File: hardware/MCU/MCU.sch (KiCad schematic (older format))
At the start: 27 parts, among them P1 CONN_01X05, P2 CONN_01X04, P3 CONN_01X03, U1 MAX6369, U2 DS18B20, U3 PIC18F45K22, U4 LM358, Y1 Crystal

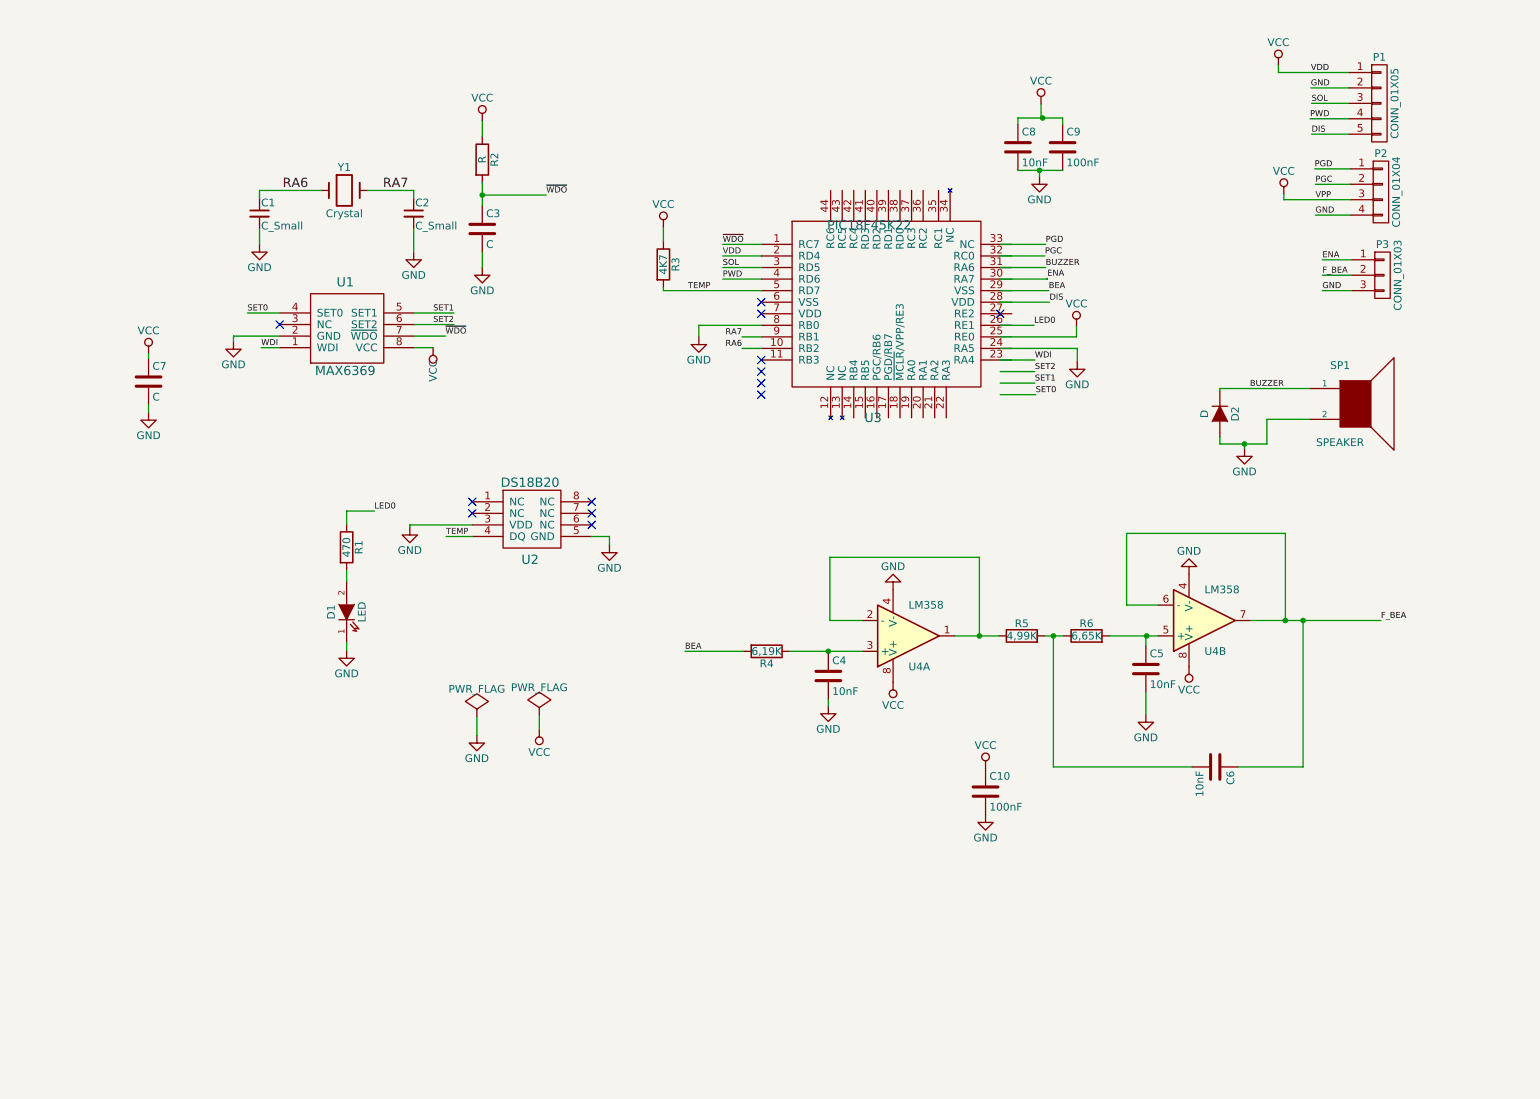
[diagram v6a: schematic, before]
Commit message: PIC schematic of 64 pins. Reorganized pinout
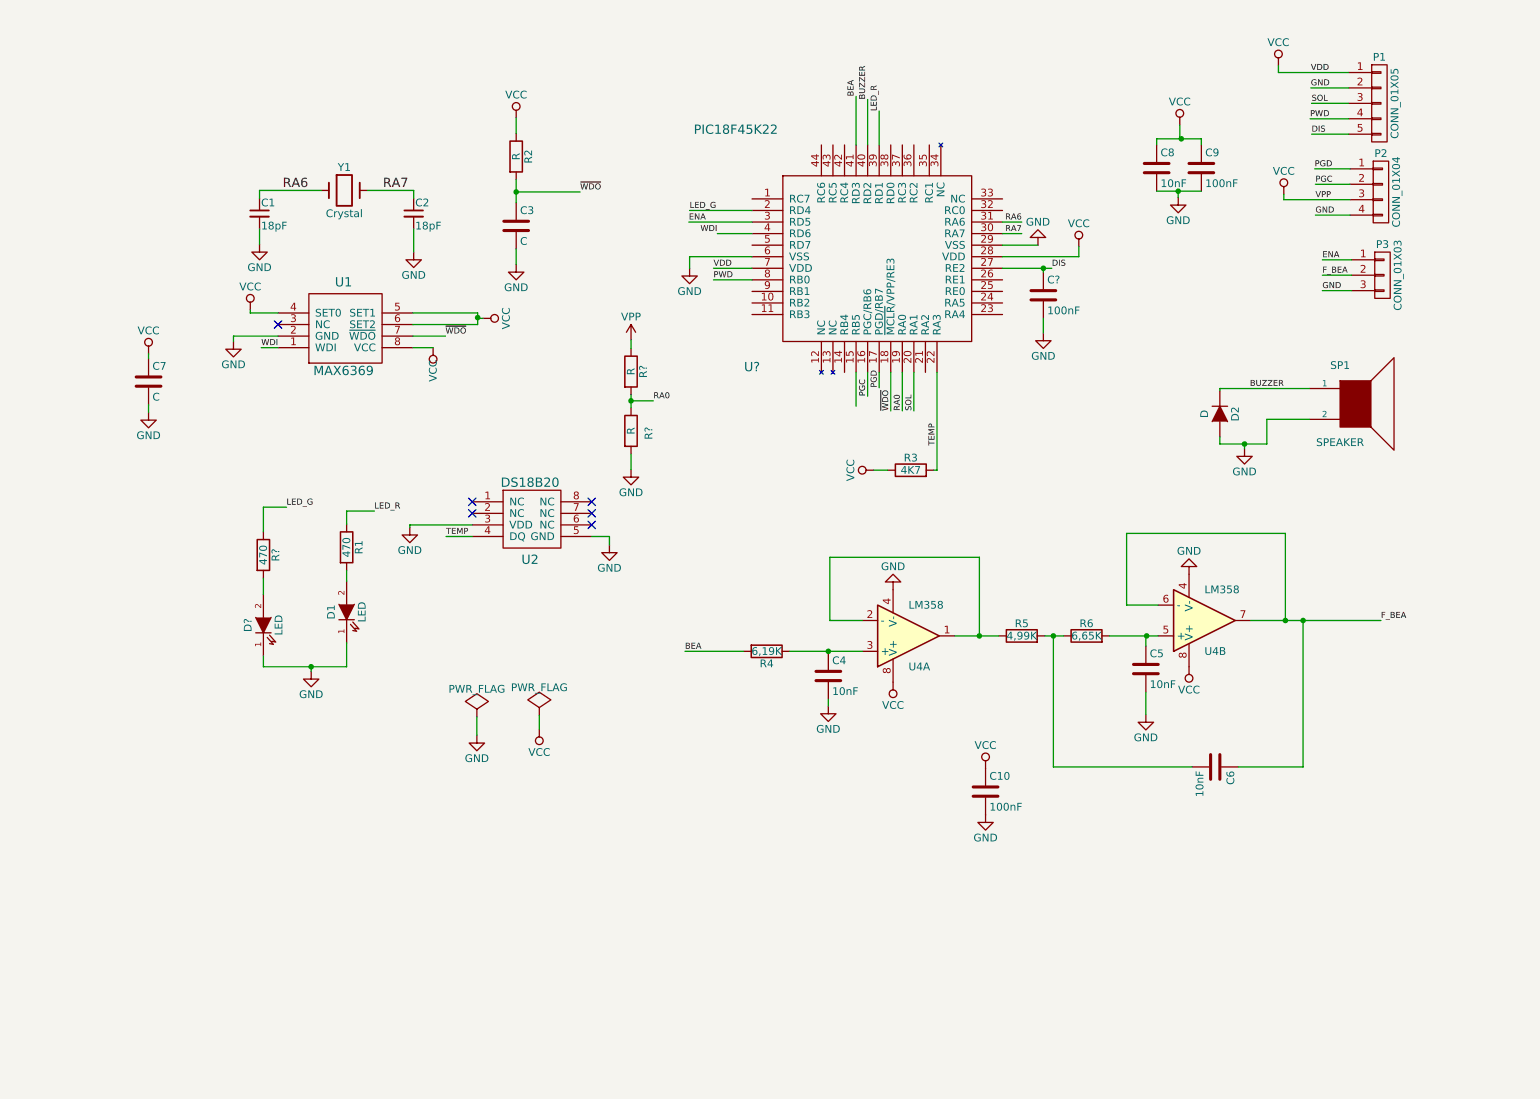
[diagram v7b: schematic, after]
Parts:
- removed U3: PIC18F45K22, Housings_SOIC:SOIC-28W_7.5x17.9mm_Pitch1.27mm, symbol PIC18F45K22
- added C?: 100nF, Capacitors_SMD:C_1206_HandSoldering, symbol C
- added D?: LED, symbol LED
- added R?: 470, Resistors_SMD:R_1206_HandSoldering, symbol R
- added R? (x2): R, symbol R
- added U?: PIC18F45K22, symbol PIC18F45K22
- C1, C2: value C_Small -> 18pF
- U1: footprint Housings_SOIC:SOIJ-8_5.3x5.3mm_Pitch1.27mm -> smd-semi:SOT-23-8
- Y1: footprint Crystals:Crystal_C26-LF_d2.1mm_l6.5mm_Horizontal -> Crystals:Crystal_HC49-4H_Vertical
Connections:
- net labels added: LED_G, LED_R, RA0
- net labels removed: LED0, SET0, SET1, SET2
- wire segments 109 -> 123
- no-connect marks 13 -> 6
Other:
- moved on the sheet: C3, C8, C9, R2, R3

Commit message: Corregidas erratas en el documento de requisitos de la MCU. Añadido regulador al esquematico y ajustadas las conexiones acorde a los requisitos
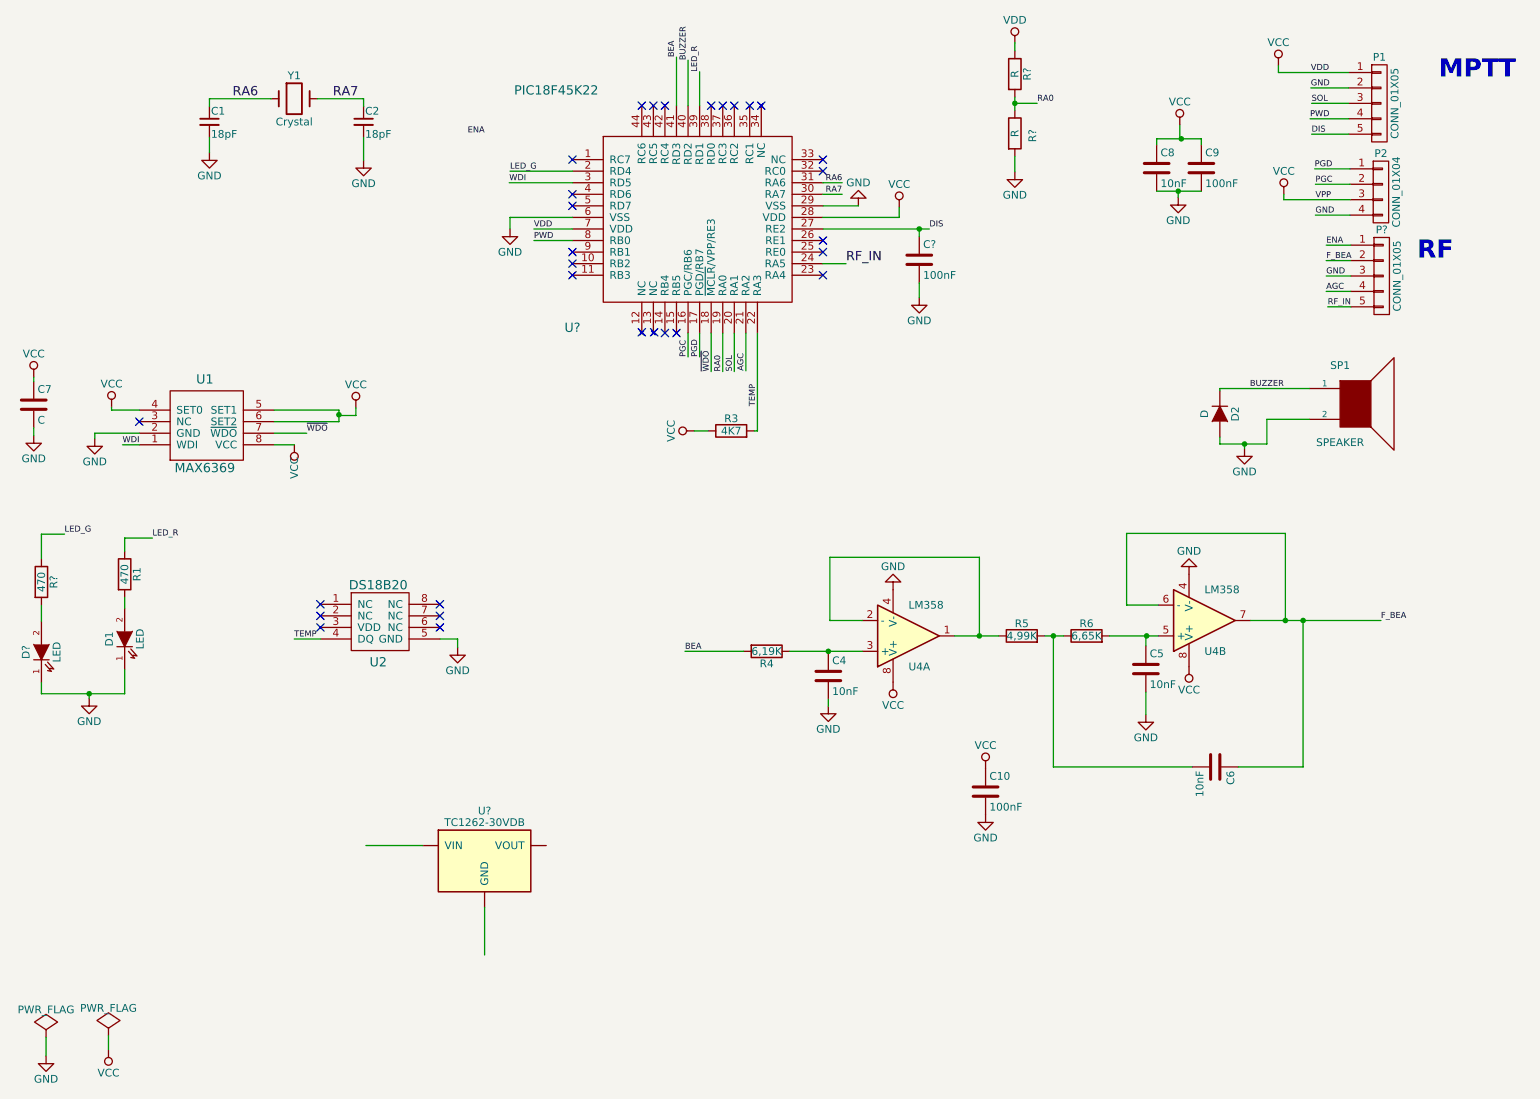
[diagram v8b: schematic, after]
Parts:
- removed C3: C, Capacitors_SMD:C_1206_HandSoldering, symbol C
- removed P3: CONN_01X03, Connectors_Terminal_Blocks:TerminalBlock_Pheonix_MPT-2.54mm_3pol, symbol CONN_01X03
- removed R2: R, Resistors_SMD:R_1206_HandSoldering, symbol R
- added P?: CONN_01X05, Connectors_Terminal_Blocks:TerminalBlock_Pheonix_MPT-2.54mm_5pol, symbol CONN_01X05
- added U?: TC1262-30VDB, SOT-223, symbol TC1262-30VDB
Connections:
- net ENA: now also P?.1 (P1); no longer U?.3 (RD5)
- net F_BEA: now also P?.2 (P2)
- net GND: now also P?.3 (P3); no longer U2.3 (VDD)
- net VCC: no longer R?.1
- net WDI: now also U?.3 (RD5); no longer U?.4 (RD6)
- net AGC: now reaches U?.21 (RA2)
- net AGC: now also P?.4 (P4)
- net RF_IN: now reaches U?.24 (RA5)
- net RF_IN: now also P?.5 (P5)
- new net: U?.2 (GND), U?.4 (GND)
- no-connect marks 6 -> 30
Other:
- note added: "MPTT"
- note added: "RF"
- moved on the sheet: C1, C2, C7, C?, D1, D?, R1, R3, R?, U1, U2, U?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
